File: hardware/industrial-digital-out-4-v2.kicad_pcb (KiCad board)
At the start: 2 copper layers, 40 x 40 mm, 38 parts, among them P1 CON-SENSOR2, P2 Digital Output, P3 DEBUG, P4 BOOT, Q1 FDN5630, U1 XMC1XXX24, U2 LTV846S, U3 OPA4171AIDR, U4 DRILL, U5 DRILL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

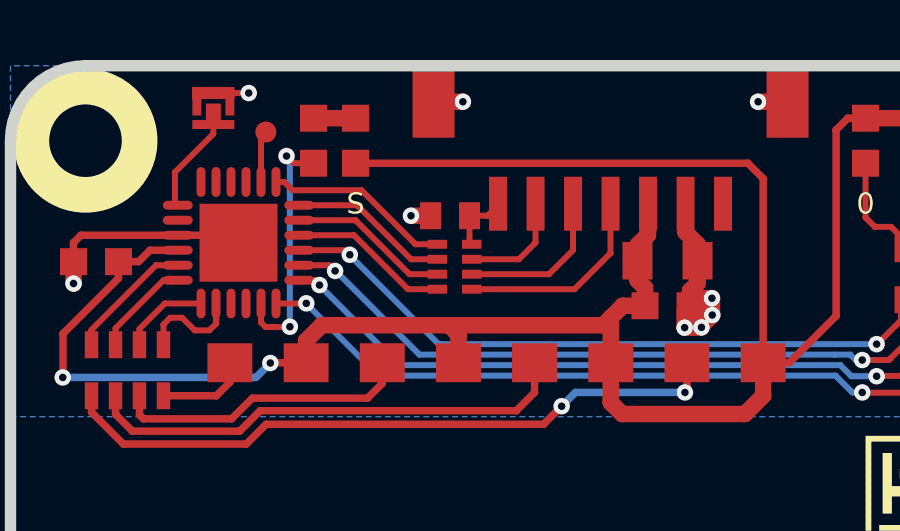
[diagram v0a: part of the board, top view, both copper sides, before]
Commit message: Change capacitor footprint(s) to C0402F
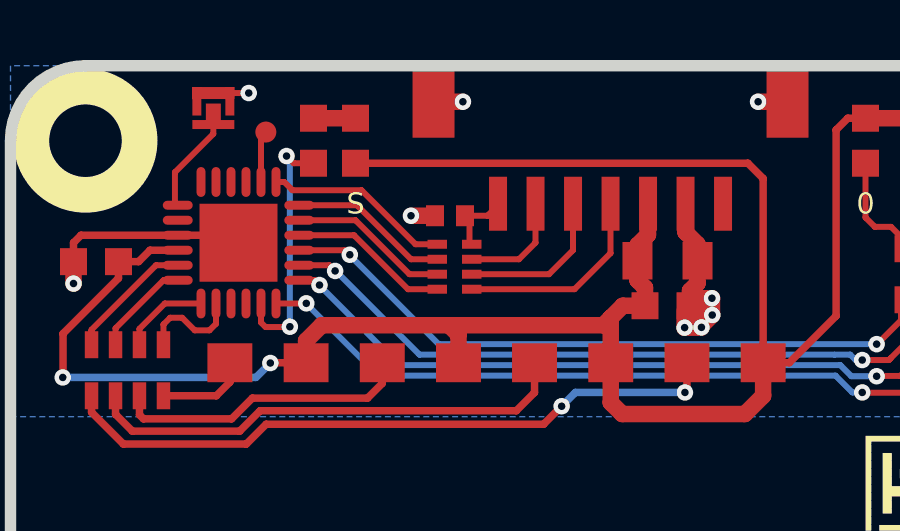
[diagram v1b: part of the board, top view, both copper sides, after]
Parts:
- C1, C2: footprint C0805 -> kicad-libraries:C0805
- C3: footprint ELKO_83 -> kicad-libraries:ELKO_83
- C4: footprint C0402E -> kicad-libraries:C0402F
- C5, C6: footprint C0603F -> kicad-libraries:C0603F
- D1: footprint MiniMelf -> kicad-libraries:MiniMelf
- D2, D3, D4, D5, D6: footprint D0603F -> kicad-libraries:D0603F
- P1: footprint CON-SENSOR2 -> kicad-libraries:CON-SENSOR2
- P2: footprint OQ_8P -> kicad-libraries:OQ_8P
- P4: footprint SolderJumper -> kicad-libraries:SolderJumper
- Q1: footprint SOT23GDS -> kicad-libraries:SOT23GDS
- R1, R2: footprint R0603F -> kicad-libraries:R0603F
- RP1, RP6: footprint 0603X4 -> kicad-libraries:0603X4
- RP2, RP3, RP4: footprint 1206X4 -> kicad-libraries:1206X4
- RP5: footprint 4X0402 -> kicad-libraries:4X0402
- U2: footprint OPTO-SMD16 -> kicad-libraries:OPTO-SMD16
- U3: footprint SOP14 -> kicad-libraries:SOP14
- U4, U5, U6, U7: footprint DRILL_NP -> kicad-libraries:DRILL_NP

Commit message: specify processor
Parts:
- U1: value XMC1XXX24 -> XMC11XX24
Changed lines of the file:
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@@
-(kicad_pcb (version 4) (host pcbnew 4.0.2+dfsg1-stable)
+(kicad_pcb (version 4) (host pcbnew 4.0.7-e2-6376~61~ubuntu18.04.1)
   (general
     (links 106)
     (no_connects 0)
-    (area 97.609659 37.858699 137.993121 78.242161)
+    (area 14.95415 37.193699 138.655581 193.940793)
     (thickness 1.6002)
     (drawings 25)
@@
       (effects (font (size 0.3 0.3) (thickness 0.075)))
     )
-    (fp_text value XMC1XXX24 (at 0 0.8 270) (layer F.Fab)
+    (fp_text value XMC11XX24 (at 0 0.8 270) (layer F.Fab)
       (effects (font (size 0.3 0.3) (thickness 0.075)))
     )
